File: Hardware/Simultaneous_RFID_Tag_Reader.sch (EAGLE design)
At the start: 37 parts, among them J2 FTDI, J3 JST, J4 U.FL, J5 Extra, J6 Screw Terminal, J7 GPIOs, U1 Nano, U2 TXB0104, U3 ESD Diode

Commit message: Fixed problems found during review
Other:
- note added: "These 3 GPIO-LV Pins are 3.3V tolerant. Do not expose them to 5V."
- note removed: "New Digikey Part: DT1042‑04SO-7DITR-ND"
- moved on the sheet: B1, C12, C2, C3, C4, C7, C8, C9, D1, D2, E2, J2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

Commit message: Finalizing antenna. Adding buzzer.
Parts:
- removed C8: ??, SparkFun-Capacitors:1.0PF-0603-50V-25%
- removed E2: Trace Antenna, UHF_RFID_Nano_Module:ANTENNA_GROUNDED1
- removed U1: Nano, UHF_RFID_Nano_Module:UHF_RFID_NANO_MODULE
- added E1: Trace Antenna, ThingMagic_Module:ANTENNA_GROUNDED1
- added L1: 3.9nH, ThingMagic_Module:3.9NH_-+0.3NH_300MA(0603)0603
- added SG1: Buzzer, ThingMagic_Module:BUZZERSMD2
- added U4: Nano, ThingMagic_Module:UHF_RFID_NANO_MODULE
- C3, C4, C7: value ?? -> DNP
- D2: value 3A/40V/500mV -> B340A
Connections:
- new net N$11: B1.*D9, SG1.1
- new net N$13: B1.*D10, SG1.2
- net 3.3V: now also U4.VOUT; no longer U1.VOUT
- net ANT3: now also U4.RF; no longer U1.RF
- net ENABLE-LV: now also U4.ENABLE; no longer U1.ENABLE
- net GND: now also E1.GND, U4.GND@1, U4.GND@18, U4.GND@19, U4.GND@2, U4.GND@29, U4.GND@3, U4.GND@30, U4.GND@31, U4.GND@32, U4.GND@33, U4.GND@34, U4.GND@35, U4.GND@36, U4.GND@37, U4.GND@38, U4.GND@4, U4.GND@40, U4.GND@41, U4.GND@5, U4.GND@6, U4.GND@7, U4.GND@8, U4.GND@9, U4.GNDP2; no longer E2.GND, U1.GND@1, U1.GND@18, U1.GND@19, U1.GND@2, U1.GND@29, U1.GND@3, U1.GND@30, U1.GND@31, U1.GND@32, U1.GND@33, U1.GND@34, U1.GND@35, U1.GND@36, U1.GND@37, U1.GND@38, U1.GND@4, U1.GND@40, U1.GND@41, U1.GND@5, U1.GND@6, U1.GND@7, U1.GND@8, U1.GND@9, U1.GNDP2
- net GPIO1-LV: now also U4.GPIO1; no longer U1.GPIO1
- net GPIO2-LV: now also U4.GPIO2; no longer U1.GPIO2
- net GPIO3-LV: now also U4.GPIO3; no longer U1.GPIO3
- net GPIO4-LV: now also U4.GPIO4; no longer U1.GPIO4
- net N$1: now also E1.SIGNAL, L1.2; no longer C8.2, E2.SIGNAL
- net N$2: now also L1.1; no longer C8.1
- net N$4: now also U4.RFU@26; no longer U1.RFU@26
- net RXI-LV: now also U4.UART_RX; no longer U1.UART_RX
- net TXO-LV: now also U4.UART_TX; no longer U1.UART_TX
- net VCC: now also U4.VIN@16, U4.VIN@17; no longer U1.VIN@16, U1.VIN@17
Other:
- note added: "Added thermals to user solderable GND connections"
- note added: "Changes on v10:"
- note added: "Decreased size of RF pad to avoid GND pad on module."
- note added: "Finalized trace antenna design and matching network"
- note added: "Lack of thermals makes soldering hard - add thermals to all gnd solder connections"
- note added: "v10"
- note removed: "v01"

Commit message: Added heat sink area and mounting holes.
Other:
- note added: "Caution: Module gets hot when reading at full power"
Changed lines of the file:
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@@
 <?xml version="1.0" encoding="utf-8"?>
 <!DOCTYPE eagle SYSTEM "eagle.dtd">
-<eagle version="7.2.0">
+<eagle version="7.5.0">
 <drawing>
 <settings>
@@
 <text x="436.88" y="271.78" size="2.54" layer="97">Changes on v10:</text>
 <text x="441.96" y="256.54" size="2.54" layer="97">Added thermals to user solderable GND connections</text>
+<text x="129.54" y="111.76" size="1.778" layer="97">Caution: Module gets hot
+when reading at full power</text>
 </plain>
 <instances>

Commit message: Adding buzzer labels
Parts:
- added STANDOFF7, STANDOFF8: STAND-OFF, SparkFun-Electromechanical:STAND-OFF
- C4, C7: value DNP -> TBD
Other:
- note added: "Decreased size of RF pad to avoid GND pad on module"
- note added: "Opened up heatsink area on bottom of PCB"
- note added: "These 3 GPIO-LV pins are 3.3V tolerant. Do not expose them to 5V."
- note removed: "Decreased size of RF pad to avoid GND pad on module."
- note removed: "Lack of thermals makes soldering hard - add thermals to all gnd solder connections"
- note removed: "These 3 GPIO-LV Pins are 3.3V tolerant. Do not expose them to 5V."
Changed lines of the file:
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@@
 <?xml version="1.0" encoding="utf-8"?>
 <!DOCTYPE eagle SYSTEM "eagle.dtd">
-<eagle version="7.5.0">
+<eagle version="7.6.0">
 <drawing>
 <settings>
@@
 <part name="GND4" library="SparkFun-Aesthetics" deviceset="GND" device=""/>
 <part name="C3" library="SparkFun-Capacitors" deviceset="1.0PF" device="-0603-50V-25%" value="DNP"/>
-<part name="C4" library="SparkFun-Capacitors" deviceset="1.0PF" device="-0603-50V-25%" value="DNP"/>
-<part name="C7" library="SparkFun-Capacitors" deviceset="1.0PF" device="-0603-50V-25%" value="DNP"/>
+<part name="C4" library="SparkFun-Capacitors" deviceset="1.0PF" device="-0603-50V-25%" value="TBD"/>
+<part name="C7" library="SparkFun-Capacitors" deviceset="1.0PF" device="-0603-50V-25%" value="TBD"/>
 <part name="GND5" library="SparkFun-Aesthetics" deviceset="GND" device=""/>
 <part name="D1" library="SparkFun-LED" deviceset="LED-RED" device="0603" value="RED"/>
@@
 <part name="E1" library="ThingMagic_Module" deviceset="ANTENNA_GROUNDED" device="1" value="Trace Antenna"/>
 <part name="SG1" library="ThingMagic_Module" deviceset="BUZZER" device="SMD2" value="Buzzer"/>
+<part name="STANDOFF7" library="SparkFun-Electromechanical" deviceset="STAND-OFF" device=""/>
+<part name="STANDOFF8" library="SparkFun-Electromechanical" deviceset="STAND-OFF" device=""/>
 </parts>
 <sheets>
@@
 <vertex x="124.46" y="211.582" curve="-90"/>
 </polygon>
-<text x="381" y="182.88" size="1.778" layer="97">These 3 GPIO-LV Pins are
+<text x="381" y="182.88" size="1.778" layer="97">These 3 GPIO-LV pins are
 3.3V tolerant. Do not expose
 them to 5V.</text>
-<text x="63.5" y="259.08" size="1.778" layer="91">Lack of thermals makes soldering hard - add thermals to all gnd solder connections</text>
-<text x="441.96" y="266.7" size="2.54" layer="97">Decreased size of RF pad to avoid GND pad on module.</text>
-<text x="441.96" y="261.62" size="2.54" layer="97">Finalized trace antenna design and matching network</text>
-<text x="436.88" y="271.78" size="2.54" layer="97">Changes on v10:</text>
-<text x="441.96" y="256.54" size="2.54" layer="97">Added thermals to user solderable GND connections</text>
+<text x="10.16" y="40.64" size="2.54" layer="97">Decreased size of RF pad to avoid GND pad on module</text>
+<text x="10.16" y="35.56" size="2.54" layer="97">Finalized trace antenna design and matching network</text>
+<text x="5.08" y="45.72" size="2.54" layer="97">Changes on v10:</text>
+<text x="10.16" y="30.48" size="2.54" layer="97">Added thermals to user solderable GND connections</text>
 <text x="129.54" y="111.76" size="1.778" layer="97">Caution: Module gets hot
 when reading at full power</text>
+<text x="10.16" y="25.4" size="2.54" layer="97">Opened up heatsink area on bottom of PCB</text>
 </plain>
 <instances>
@@
 <instance part="FID1" gate="G$1" x="416.56" y="38.1"/>
 <instance part="FID2" gate="G$1" x="416.56" y="43.18"/>
-<instance part="LOGO1" gate="G$1" x="86.36" y="2.54"/>
-<instance part="LOGO2" gate="G$1" x="66.04" y="15.24"/>
+<instance part="LOGO1" gate="G$1" x="271.78" y="2.54"/>
+<instance part="LOGO2" gate="G$1" x="251.46" y="15.24"/>
 <instance part="R3" gate="G$1" x="144.78" y="147.32"/>
 <instance part="U2" gate="G$1" x="304.8" y="236.22"/>
@@
 <instance part="GND21" gate="1" x="119.38" y="114.3"/>
 <instance part="C2" gate="G$1" x="55.88" y="134.62"/>
-<instance part="LOGO3" gate="G$1" x="86.36" y="2.54"/>
+<instance part="LOGO3" gate="G$1" x="271.78" y="2.54"/>
 <instance part="J7" gate="J$1" x="406.4" y="200.66" rot="MR0"/>
 <instance part="TP1" gate="G$1" x="88.9" y="152.4" smashed="yes" rot="R90">
@@
 <attribute name="VALUE" x="312.674" y="86.868" size="1.778" layer="96"/>
 </instance>
+<instance part="STANDOFF7" gate="G$1" x="421.64" y="48.26"/>
+<instance part="STANDOFF8" gate="G$1" x="426.72" y="48.26"/>
 </instances>
 <busses>

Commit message: Changing input silk to 3.7-5V.
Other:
- note added: "Internal DC-DC will use the following (Max): 720mA @ 5V 972mA @ 3.7V"
- note added: "This buffer does not operate when VCCA > VCCB. VCC must be greater than 3.3V."
- note added: "VCC must be 3.7-5.5V"
- note removed: "Internal DC-DC will use the following (Max): 720mA @ 5V 972mA @ 3.7V 1091mA @ 3.3V"
- note removed: "VCC must be 3.3-5.5V"
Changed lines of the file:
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@@
 <?xml version="1.0" encoding="utf-8"?>
 <!DOCTYPE eagle SYSTEM "eagle.dtd">
-<eagle version="7.6.0">
+<eagle version="7.5.0">
 <drawing>
 <settings>
@@
 <wire x1="220.98" y1="279.4" x2="220.98" y2="177.8" width="0.2032" layer="97" style="longdash"/>
 <text x="304.8" y="182.88" size="2.54" layer="97" align="center">Interface and Logic Conversion</text>
-<text x="281.94" y="167.64" size="2.54" layer="97">VCC must be 3.3-5.5V</text>
+<text x="281.94" y="167.64" size="2.54" layer="97">VCC must be 3.7-5.5V</text>
 <text x="335.28" y="147.32" size="1.778" layer="97">Internal DC-DC will use the
 following (Max):
     720mA @ 5V
     972mA @ 3.7V
-    1091mA @ 3.3V</text>
+</text>
 <text x="116.84" y="101.6" size="2.54" layer="97" align="center">RFID Module</text>
 <text x="83.82" y="220.98" size="1.778" layer="97">SJ1 and SJ2 select
@@
 when reading at full power</text>
 <text x="10.16" y="25.4" size="2.54" layer="97">Opened up heatsink area on bottom of PCB</text>
+<text x="312.42" y="210.82" size="1.778" layer="97">This buffer does not operate
+when VCCA &gt; VCCB. VCC must
+be greater than 3.3V.</text>
 </plain>
 <instances>

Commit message: Finishing matching network to u.FL
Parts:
- C4: value TBD -> DNP
- C7: value TBD -> 0.0
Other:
- moved on the sheet: C7
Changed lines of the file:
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@@
 <?xml version="1.0" encoding="utf-8"?>
 <!DOCTYPE eagle SYSTEM "eagle.dtd">
-<eagle version="7.5.0">
+<eagle version="7.2.0">
 <drawing>
 <settings>
@@
 <part name="GND4" library="SparkFun-Aesthetics" deviceset="GND" device=""/>
 <part name="C3" library="SparkFun-Capacitors" deviceset="1.0PF" device="-0603-50V-25%" value="DNP"/>
-<part name="C4" library="SparkFun-Capacitors" deviceset="1.0PF" device="-0603-50V-25%" value="TBD"/>
-<part name="C7" library="SparkFun-Capacitors" deviceset="1.0PF" device="-0603-50V-25%" value="TBD"/>
+<part name="C4" library="SparkFun-Capacitors" deviceset="1.0PF" device="-0603-50V-25%" value="DNP"/>
+<part name="C7" library="SparkFun-Capacitors" deviceset="1.0PF" device="-0603-50V-25%" value="0.0"/>
 <part name="GND5" library="SparkFun-Aesthetics" deviceset="GND" device=""/>
 <part name="D1" library="SparkFun-LED" deviceset="LED-RED" device="0603" value="RED"/>
@@
 <instance part="C3" gate="G$1" x="152.4" y="213.36"/>
 <instance part="C4" gate="G$1" x="152.4" y="182.88"/>
-<instance part="C7" gate="G$1" x="147.32" y="190.5" rot="R90"/>
+<instance part="C7" gate="G$1" x="134.62" y="190.5" rot="R90"/>
 <instance part="GND5" gate="1" x="152.4" y="175.26"/>
 <instance part="D1" gate="G$1" x="43.18" y="137.16"/>
@@
 <pinref part="SJ2" gate="G$1" pin="2"/>
 <wire x1="124.46" y1="193.04" x2="124.46" y2="190.5" width="0.1524" layer="91"/>
-<wire x1="124.46" y1="190.5" x2="142.24" y2="190.5" width="0.1524" layer="91"/>
+<wire x1="124.46" y1="190.5" x2="129.54" y2="190.5" width="0.1524" layer="91"/>
 <pinref part="C7" gate="G$1" pin="1"/>
 </segment>
@@
 <pinref part="C7" gate="G$1" pin="2"/>
 <pinref part="C4" gate="G$1" pin="1"/>
-<wire x1="149.86" y1="190.5" x2="152.4" y2="190.5" width="0.1524" layer="91"/>
+<wire x1="137.16" y1="190.5" x2="152.4" y2="190.5" width="0.1524" layer="91"/>
 <wire x1="152.4" y1="190.5" x2="152.4" y2="187.96" width="0.1524" layer="91"/>
 <wire x1="152.4" y1="190.5" x2="154.94" y2="190.5" width="0.1524" layer="91"/>

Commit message: Adding cosmetic GND connection to schematic.
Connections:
- net GND: now also U4.GNDP1
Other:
- note added: "Internal DC-DC will use the following: 900mA @ 5V 1100mA @ 3.7V"
- note removed: "Internal DC-DC will use the following (Max): 720mA @ 5V 972mA @ 3.7V"
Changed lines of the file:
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@@
 <?xml version="1.0" encoding="utf-8"?>
 <!DOCTYPE eagle SYSTEM "eagle.dtd">
-<eagle version="7.2.0">
+<eagle version="7.6.0">
 <drawing>
 <settings>
@@
 <part name="STANDOFF7" library="SparkFun-Electromechanical" deviceset="STAND-OFF" device=""/>
 <part name="STANDOFF8" library="SparkFun-Electromechanical" deviceset="STAND-OFF" device=""/>
+<part name="GND22" library="SparkFun-Aesthetics" deviceset="GND" device=""/>
 </parts>
 <sheets>
@@
 <text x="281.94" y="167.64" size="2.54" layer="97">VCC must be 3.7-5.5V</text>
 <text x="335.28" y="147.32" size="1.778" layer="97">Internal DC-DC will use the
-following (Max):
-    720mA @ 5V
-    972mA @ 3.7V
+following:
+    900mA @ 5V
+    1100mA @ 3.7V
 </text>
 <text x="116.84" y="101.6" size="2.54" layer="97" align="center">RFID Module</text>
@@
 <instance part="STANDOFF7" gate="G$1" x="421.64" y="48.26"/>
 <instance part="STANDOFF8" gate="G$1" x="426.72" y="48.26"/>
+<instance part="GND22" gate="1" x="114.3" y="114.3"/>
 </instances>
 <busses>
@@
 <pinref part="U4" gate="U1" pin="GNDP2"/>
 </segment>
+<segment>
+<pinref part="U4" gate="U1" pin="GNDP1"/>
+<pinref part="GND22" gate="1" pin="GND"/>
+<wire x1="114.3" y1="124.46" x2="114.3" y2="116.84" width="0.1524" layer="91"/>
+</segment>
 </net>

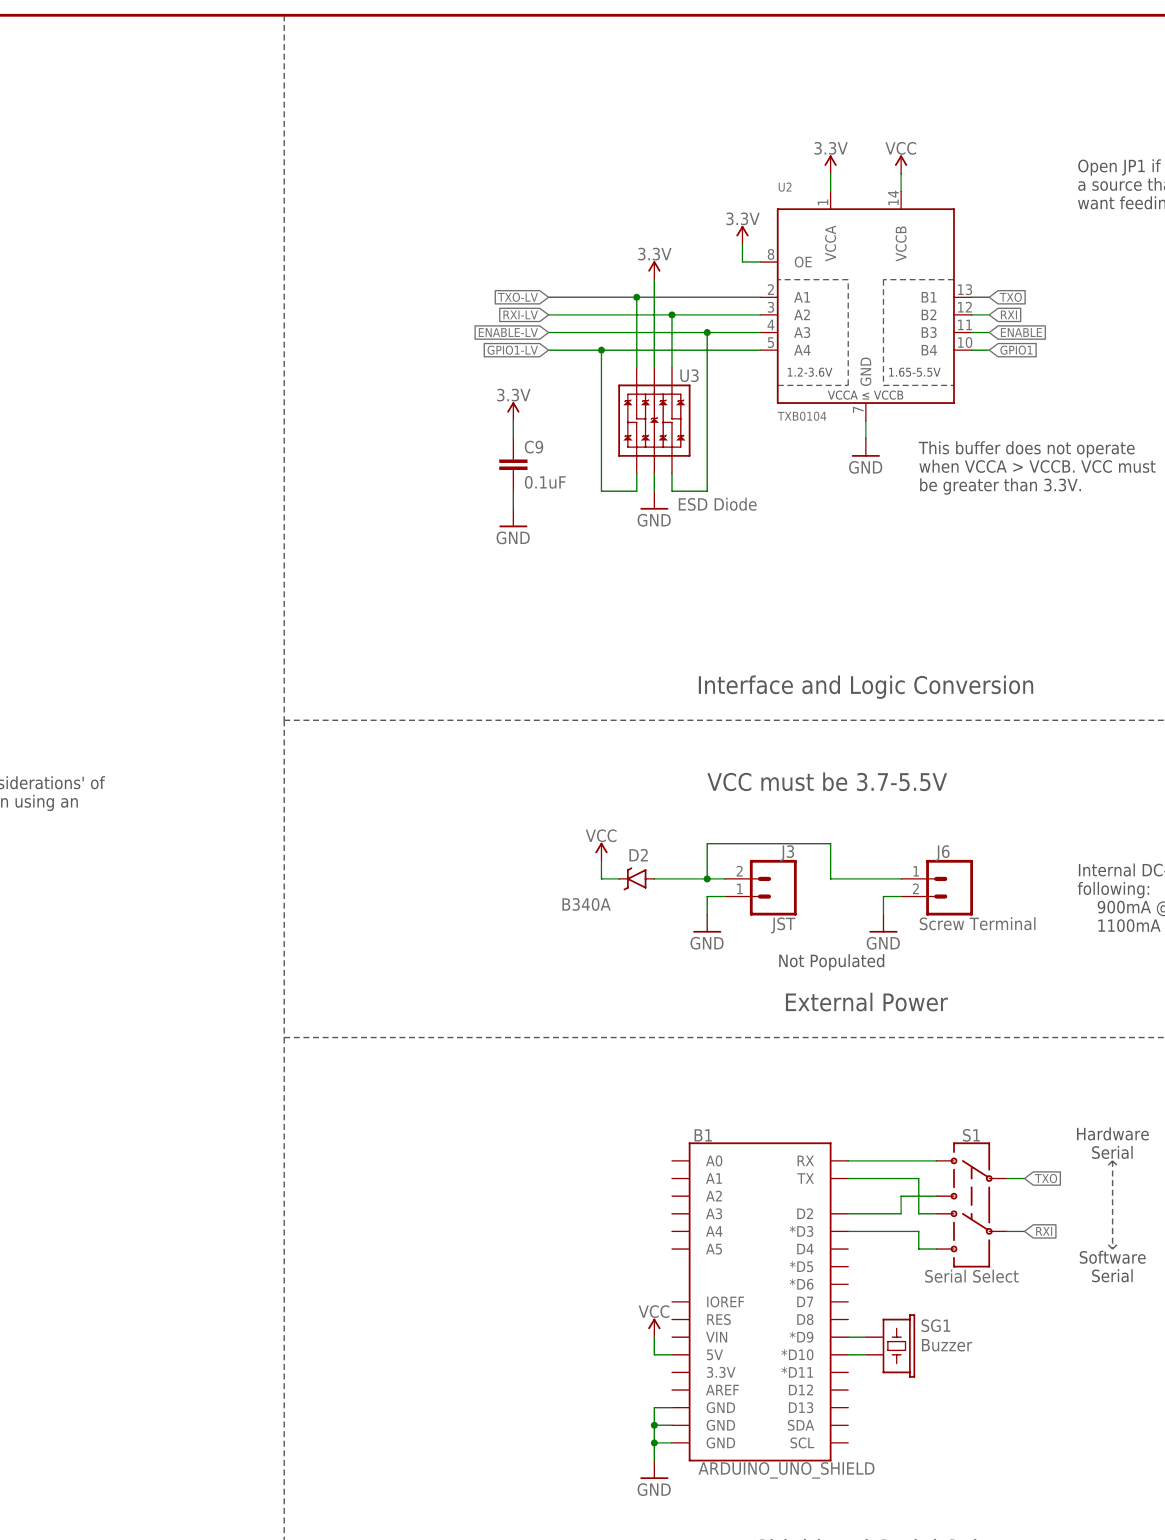
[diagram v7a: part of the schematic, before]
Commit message: Added insulation to ISP and ground thermal. Added RF supressors to enable. Grounded half of buzzer.
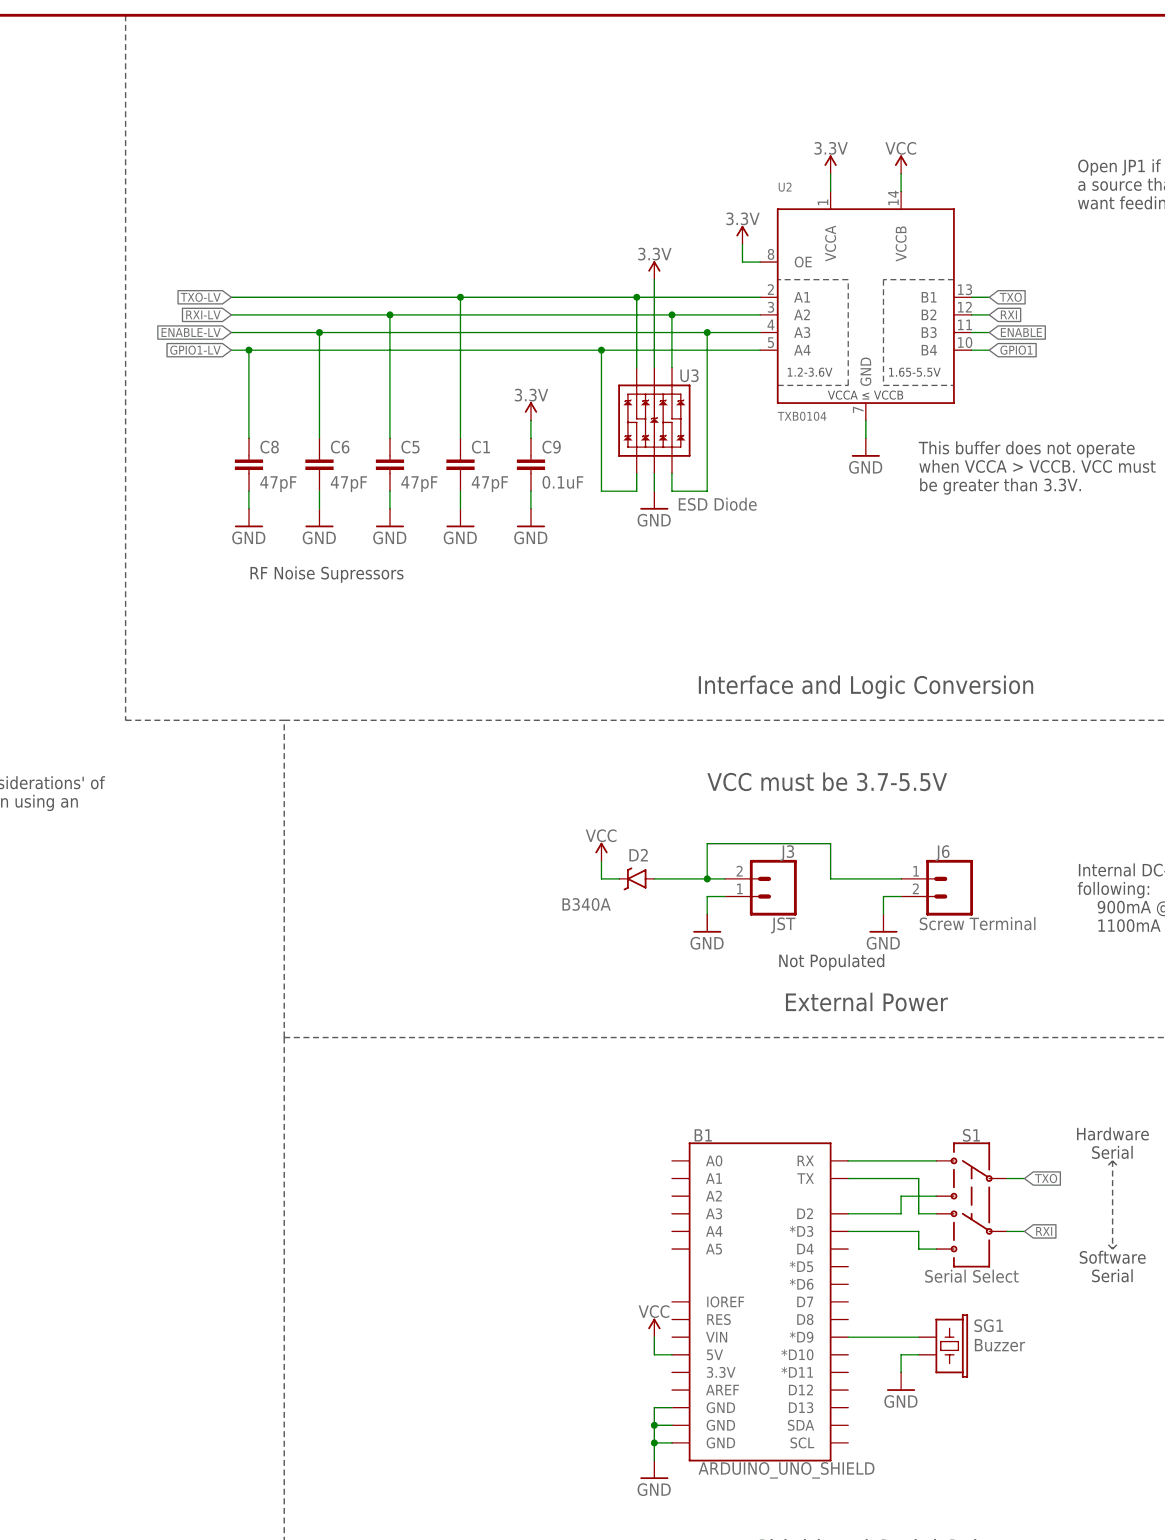
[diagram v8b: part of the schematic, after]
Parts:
- added C1, C5, C6, C8: 47pF, SparkFun-Capacitors:47PF-0603-50V-5%
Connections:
- removed net N$13: B1.*D10, SG1.2
- net ENABLE-LV: now also C6.1
- net GND: now also C1.2, C5.2, C6.2, C8.2, SG1.2
- net GPIO1-LV: now also C8.1
- net RXI-LV: now also C5.1
- net TXO-LV: now also C1.1
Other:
- note added: "RF Noise Supressors"
- moved on the sheet: C9, SG1
